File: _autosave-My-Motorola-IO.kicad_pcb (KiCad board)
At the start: 2 copper layers, 99.8 x 99.8 mm, 37 parts, among them J1 MECB_64AC, J2 PS/2_Connector, J6 Conn_02x12_Odd_Even, P1 FTDI_con, Q1 2N7000, Q2 2N7000, U1 ATF16V8, U2 RTC72421, U4 SCC2691, U5 WD65C22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

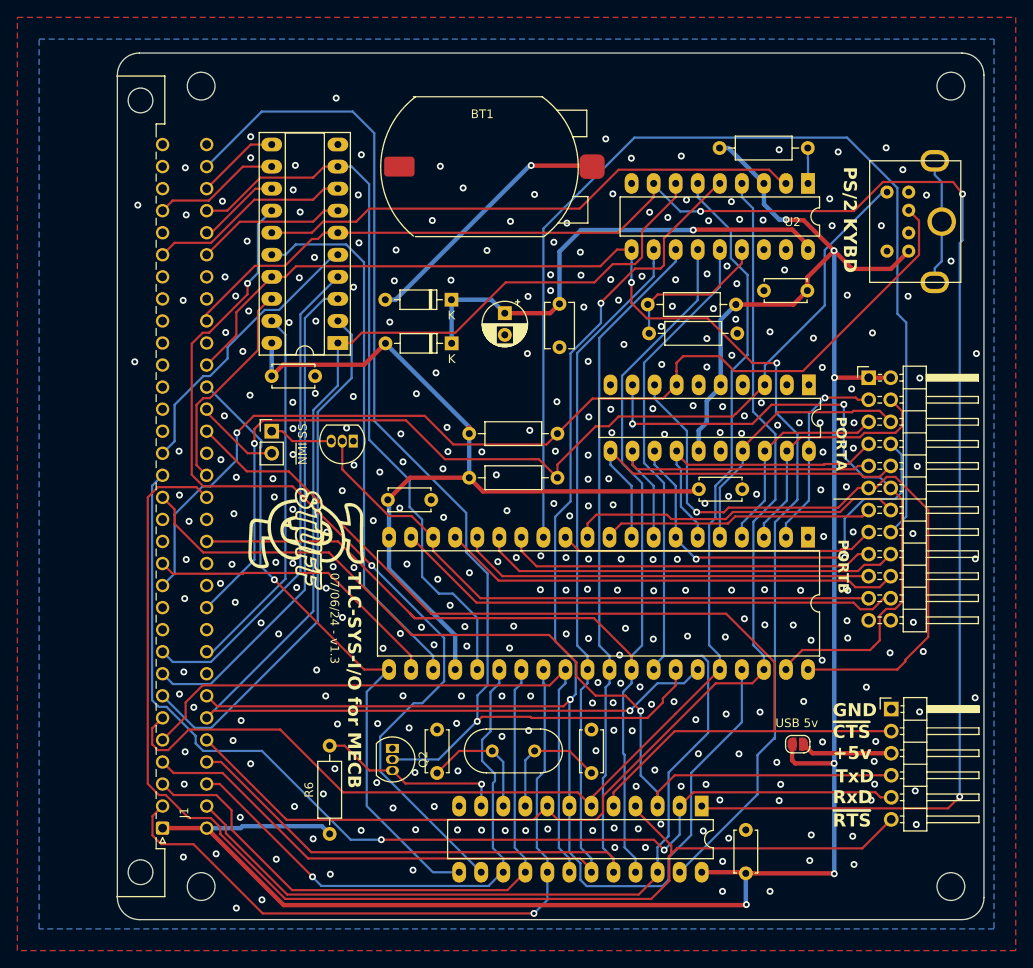
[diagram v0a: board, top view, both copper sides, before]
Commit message: updated SCC2691 reset line and battery holder
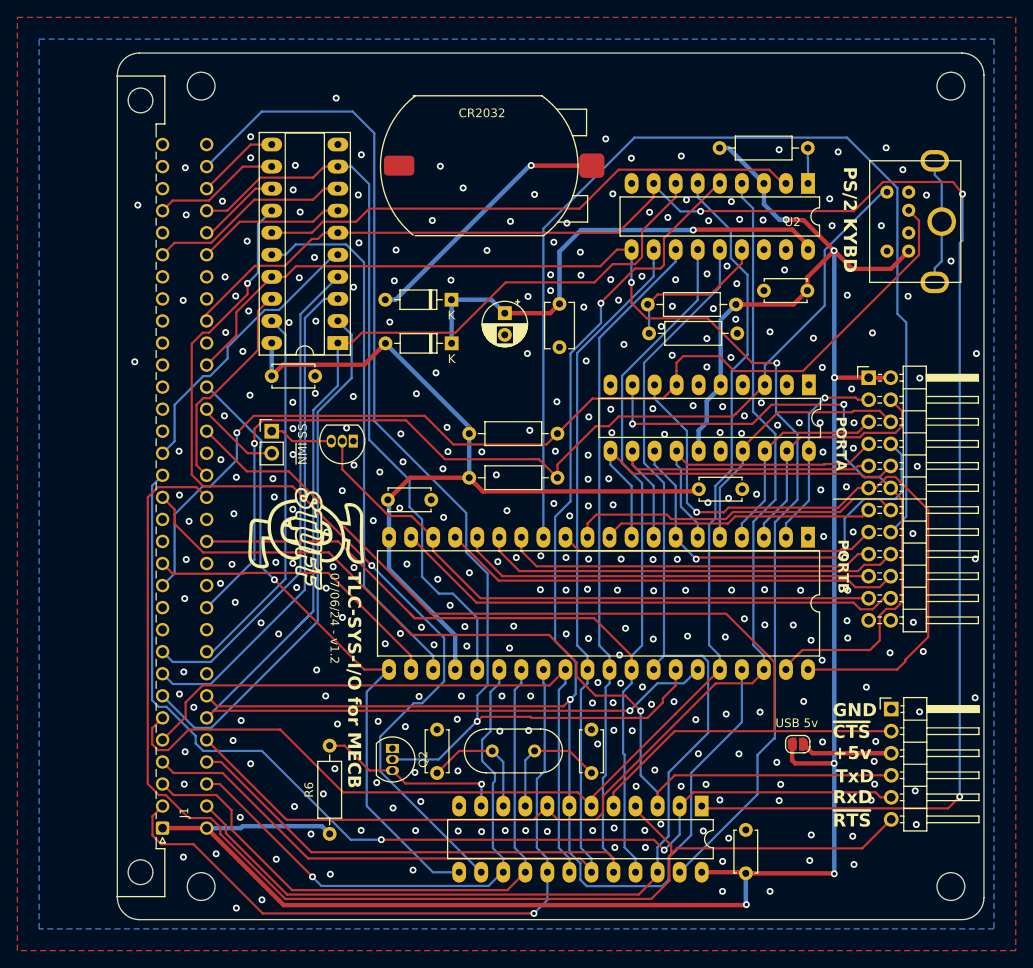
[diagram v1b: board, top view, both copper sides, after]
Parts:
- removed BT1: Battery_Cell, TLC_Stuff:SMD CR2032
- added CR2032: 3.6v, TLC_Stuff:SMD CR2032, F.Cu at (139.6, 59.6)
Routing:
- net ECB_A3: track 157.5 -> 161.7 mm
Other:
- board text added: "07/06/24 - v1.2"
- board text removed: "07/06/24 - v1.3"
